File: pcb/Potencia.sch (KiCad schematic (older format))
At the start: 32 parts, among them U3 L298, U4 L298

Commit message: carga de hojas jerarquia
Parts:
- added HS1, HS2: HEATSINK, symbol HEATSINK
- C4, C6, C7, C9: Fabricante (none) -> avx; Provedor (none) -> tme; Ref (none) -> 08055C104K4T2A; Ref_Proveedor (none) -> 08055C104K4T2A
- C5, C8: Provedor (none) -> tme; Ref_Proveedor (none) -> EEVFK1J471M
- D10, D11, D12, D13, D14, D15, D16, D17, D18, D3, D4, D5, D6, D7, D8, D9: Fabricante (none) -> vishay; Provedor (none) -> tme; Ref (none) -> 10MQ100NTRPBF; Ref_Proveedor (none) -> 10MQ100NTRPBF
- R10, R11, R6, R7: Fabricante (none) -> vishay; Potencia (none) -> 0.125W; Provedor (none) -> tme; Ref (none) -> CRCW080510K0FKEA; Ref_Proveedor (none) -> CRCW080510K0FKEA; Tolerancia (none) -> 1%
- R12, R13, R8, R9: Fabricante (none) -> walsin; Potencia (none) -> 1W; Provedor (none) -> tme; Ref (none) -> WW12DR020FTL; Ref_Proveedor (none) -> WW12DR020FTL; Tolerancia (none) -> 1%
- U3, U4: Fabricante (none) -> st; Provedor (none) -> tme; Ref (none) -> L298N; Ref_Proveedor (none) -> L298N
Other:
- moved on the sheet: C4, C5, C6, C7, C8, C9, D10, D11, D12, D13, D14, D15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

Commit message: finalizada realizacion de esquema
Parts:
- added C10, C11, C12, C16, C17, C18, C19, C9: 1,5n, symbol C
- added D15, D16, D17, D18, D3, D4, D5, D6: 1N4148, symbol D
- added R11, R12, R13, R14, R17, R18, R19, R20: 10K, symbol R
- D10: renamed from D6; value D -> 10MQ100
- D11: renamed from D7; value D -> 10MQ100
- D12: renamed from D8; value D -> 10MQ100
- D13: renamed from D9; value D -> 10MQ100
- D14: renamed from D10; value D -> 10MQ100
- D19: renamed from D11; value D -> 10MQ100
- D20: renamed from D12; value D -> 10MQ100
- D21: renamed from D13; value D -> 10MQ100
- D22: renamed from D14; value D -> 10MQ100
- D23: renamed from D15; value D -> 10MQ100
- D24: renamed from D16; value D -> 10MQ100
- D25: renamed from D17; value D -> 10MQ100
- D26: renamed from D18; value D -> 10MQ100
- D7: renamed from D3; value D -> 10MQ100
- D8: renamed from D4; value D -> 10MQ100
- D9: renamed from D5; value D -> 10MQ100
- renumbered C4 to C13, C5 to C14, C6 to C15, C7 to C20, C8 to C21, C9 to C22, R7 to R10, R8 to R15, R9 to R16, R10 to R21, R11 to R22, R12 to R23, R13 to R24, R6 to R9, U3 to U4, U4 to U5
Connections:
- net labels added: Motor1_A_in, Motor1_B_in, Motor2_A_in, Motor2_B_in, Motor3_A_in, Motor3_B_in, Motor4_A_in, Motor4_B_in
- wire segments 90 -> 146
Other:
- moved on the sheet: C13, C14, C15, C20, C21, C22, D10, D11, D12, D13, D14, D19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

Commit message: asociacion de huellas a resistencias y condensadores
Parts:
- C10, C11, C12, C13, C15, C16, C17, C18, C19, C20, C22, C9: footprint (none) -> Capacitors_SMD:C_0805
- C14: Fabricante (none) -> PANASONIC; Ref (none) -> EEVFK1J471M
- R10, R11, R12, R13, R14, R17, R18, R19, R20, R21, R22, R9: footprint (none) -> Resistors_SMD:R_0805
- R15, R16, R23, R24: value R -> 0.02; footprint (none) -> Resistors_SMD:R_1206
- U4, U5: footprint (none) -> MotorDrivers:L298_Multiwatt15V

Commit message: cambiado CI 298N por 298P por altura dentro de posible caja
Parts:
- removed U4, U5: L298, MotorDrivers:L298_Multiwatt15V, symbol L298
- added U4, U5: L298P, MotorDrivers:L298_PowerSO20, symbol L298_SO
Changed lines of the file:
@@
 Comment4 ""
 $EndDescr
-$Comp
-L L298 U4
-U 1 1 5768BA06
-P 2350 3650
-F 0 "U4" H 2900 4400 60  0000 C CNN
-F 1 "L298" H 2900 4550 60  0000 C CNN
-F 2 "MotorDrivers:L298_Multiwatt15V" H 2350 3650 60  0001 C CNN
-F 3 "" H 2350 3650 60  0000 C CNN
-F 4 "st" H 2000 1500 60  0001 C CNN "Fabricante"
-F 5 "L298N" H 2000 1500 60  0001 C CNN "Ref"
-F 6 "~" H 2000 1500 60  0001 C CNN "Potencia"
-F 7 "~" H 2000 1500 60  0001 C CNN "Tolerancia"
-F 8 "tme" H 2000 1500 60  0001 C CNN "Provedor"
-F 9 "L298N" H 2000 1500 60  0001 C CNN "Ref_Proveedor"
-	1    2350 3650
-	1    0    0    -1
-$EndComp
-$Comp
-L L298 U5
-U 1 1 5768BB47
-P 7500 3650
-F 0 "U5" H 8050 4400 60  0000 C CNN
-F 1 "L298" H 8050 4550 60  0000 C CNN
-F 2 "MotorDrivers:L298_Multiwatt15V" H 7500 3650 60  0001 C CNN
-F 3 "" H 7500 3650 60  0000 C CNN
-F 4 "st" H 1800 1500 60  0001 C CNN "Fabricante"
-F 5 "L298N" H 1800 1500 60  0001 C CNN "Ref"
-F 6 "~" H 1800 1500 60  0001 C CNN "Potencia"
-F 7 "~" H 1800 1500 60  0001 C CNN "Tolerancia"
-F 8 "tme" H 1800 1500 60  0001 C CNN "Provedor"
-F 9 "L298N" H 1800 1500 60  0001 C CNN "Ref_Proveedor"
-	1    7500 3650
-	1    0    0    -1
-$EndComp
 Text GLabel 5050 3100 2    60   Input ~ 0
 Motor2-
@@
 	1    0    0    -1
 $EndComp
+$Comp
+L L298_SO U4
+U 1 1 5771BE9E
+P 2350 3650
+F 0 "U4" H 2450 5350 60  0000 C CNN
+F 1 "L298P" H 2900 4500 60  0000 C CNN
+F 2 "MotorDrivers:L298_PowerSO20" H 2350 3650 60  0001 C CNN
+F 3 "" H 2350 3650 60  0000 C CNN
+F 4 "ST" H 2350 3650 60  0001 C CNN "Fabricante"
+F 5 "L298P" H 2350 3650 60  0001 C CNN "Ref"
+F 6 "~" H 2350 3650 60  0001 C CNN "Potencia"
+F 7 "~" H 2350 3650 60  0001 C CNN "Tolerancia"
+F 8 "tme" H 2350 3650 60  0001 C CNN "Provedor"
+F 9 "L298P" H 2350 3650 60  0001 C CNN "Ref_Proveedor"
+	1    2350 3650
+	1    0    0    -1
+$EndComp
+$Comp
+L L298_SO U5
+U 1 1 5771C16D
+P 7500 3650
+F 0 "U5" H 7600 5350 60  0000 C CNN
+F 1 "L298P" H 8050 4500 60  0000 C CNN
+F 2 "MotorDrivers:L298_PowerSO20" H 7500 3650 60  0001 C CNN
+F 3 "" H 7500 3650 60  0000 C CNN
+F 4 "ST" H 7500 3650 60  0001 C CNN "Fabricante"
+F 5 "L298P" H 7500 3650 60  0001 C CNN "Ref"
+F 6 "~" H 7500 3650 60  0001 C CNN "Potencia"
+F 7 "~" H 7500 3650 60  0001 C CNN "Tolerancia"
+F 8 "tme" H 7500 3650 60  0001 C CNN "Provedor"
+F 9 "L298P" H 7500 3650 60  0001 C CNN "Ref_Proveedor"
+	1    7500 3650
+	1    0    0    -1
+$EndComp

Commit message: añadidas asociaciones de condensadores y led
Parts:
- C14: value 470u -> 220u; footprint (none) -> Capacitors_SMD:c_elec_10x10; Ref EEVFK1J471M -> SC1H227M10010VR; Ref_Proveedor EEVFK1J471M -> SC1H227M10010VR
- C21: value 470u -> 220u; footprint (none) -> Capacitors_SMD:c_elec_10x10; Fabricante (none) -> SAMWHA; Ref (none) -> SC1H227M10010VR; Ref_Proveedor EEVFK1J471M -> SC1H227M10010VR
- D10, D11, D12, D13, D14, D19, D20, D21, D22, D23, D24, D25, D26, D7, D8, D9: footprint (none) -> Diodos:DO-214AC
- D15, D16, D17, D18, D3, D4, D5, D6: footprint (none) -> Diodos:SOD-123
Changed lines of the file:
@@
 F 0 "D7" V 3650 2050 50  0000 L CNN
 F 1 "10MQ100" H 3750 1900 50  0000 L CNN
-F 2 "" H 3750 2000 50  0001 C CNN
+F 2 "Diodos:DO-214AC" H 3750 2000 50  0001 C CNN
 F 3 "" H 3750 2000 50  0000 C CNN
 F 4 "vishay" H 3400 1400 60  0001 C CNN "Fabricante"
@@
 F 0 "D9" V 3900 2050 50  0000 L CNN
 F 1 "10MQ100" H 4000 1900 50  0000 L CNN
-F 2 "" H 4000 2000 50  0001 C CNN
+F 2 "Diodos:DO-214AC" H 4000 2000 50  0001 C CNN
 F 3 "" H 4000 2000 50  0000 C CNN
 F 4 "vishay" H 3400 1400 60  0001 C CNN "Fabricante"
@@
 F 0 "D11" V 4150 2050 50  0000 L CNN
 F 1 "10MQ100" H 4250 1900 50  0000 L CNN
-F 2 "" H 4250 2000 50  0001 C CNN
+F 2 "Diodos:DO-214AC" H 4250 2000 50  0001 C CNN
 F 3 "" H 4250 2000 50  0000 C CNN
 F 4 "vishay" H 3400 1400 60  0001 C CNN "Fabricante"
@@
 F 0 "D13" V 4400 2050 50  0000 L CNN
 F 1 "10MQ100" H 4500 1900 50  0000 L CNN
-F 2 "" H 4500 2000 50  0001 C CNN
+F 2 "Diodos:DO-214AC" H 4500 2000 50  0001 C CNN
 F 3 "" H 4500 2000 50  0000 C CNN
 F 4 "vishay" H 3400 1400 60  0001 C CNN "Fabricante"
@@
 F 0 "D8" V 3650 3500 50  0000 L CNN
 F 1 "10MQ100" H 3750 3350 50  0000 L CNN
-F 2 "" H 3750 3450 50  0001 C CNN
+F 2 "Diodos:DO-214AC" H 3750 3450 50  0001 C CNN
 F 3 "" H 3750 3450 50  0000 C CNN
 F 4 "vishay" H 3400 1400 60  0001 C CNN "Fabricante"
@@
 F 0 "D10" V 3900 3500 50  0000 L CNN
 F 1 "10MQ100" H 4000 3350 50  0000 L CNN
-F 2 "" H 4000 3450 50  0001 C CNN
+F 2 "Diodos:DO-214AC" H 4000 3450 50  0001 C CNN
 F 3 "" H 4000 3450 50  0000 C CNN
 F 4 "vishay" H 3400 1400 60  0001 C CNN "Fabricante"
@@
 F 0 "D12" V 4150 3500 50  0000 L CNN
 F 1 "10MQ100" H 4250 3350 50  0000 L CNN
-F 2 "" H 4250 3450 50  0001 C CNN
+F 2 "Diodos:DO-214AC" H 4250 3450 50  0001 C CNN
 F 3 "" H 4250 3450 50  0000 C CNN
 F 4 "vishay" H 3400 1400 60  0001 C CNN "Fabricante"
@@
 F 0 "D14" V 4400 3500 50  0000 L CNN
 F 1 "10MQ100" H 4500 3350 50  0000 L CNN
-F 2 "" H 4500 3450 50  0001 C CNN
+F 2 "Diodos:DO-214AC" H 4500 3450 50  0001 C CNN
 F 3 "" H 4500 3450 50  0000 C CNN
 F 4 "vishay" H 3400 1400 60  0001 C CNN "Fabricante"
@@
 P 3000 1400
 F 0 "C14" H 3118 1446 50  0000 L CNN
-F 1 "470u" H 3118 1355 50  0000 L CNN
-F 2 "" H 3038 1250 50  0001 C CNN
+F 1 "220u" H 3118 1355 50  0000 L CNN
+F 2 "Capacitors_SMD:c_elec_10x10" H 3038 1250 50  0001 C CNN
 F 3 "" H 3000 1400 50  0000 C CNN
 F 4 "PANASONIC" H 3000 1400 60  0001 C CNN "Fabricante"
-F 5 "EEVFK1J471M" H 3000 1400 60  0001 C CNN "Ref"
+F 5 "SC1H227M10010VR" H 3000 1400 60  0001 C CNN "Ref"
 F 6 "~" H 3000 1400 60  0001 C CNN "Potencia"
 F 7 "~" H 3000 1400 60  0001 C CNN "Tolerancia"
 F 8 "tme" H 3000 1400 60  0001 C CNN "Provedor"
-F 9 "EEVFK1J471M" H 3000 1400 60  0001 C CNN "Ref_Proveedor"
+F 9 "SC1H227M10010VR" H 3000 1400 60  0001 C CNN "Ref_Proveedor"
 	1    3000 1400
 	1    0    0    -1
@@
 F 0 "D19" V 8850 2050 50  0000 L CNN
 F 1 "10MQ100" H 8950 1900 50  0000 L CNN
-F 2 "" H 8950 2000 50  0001 C CNN
+F 2 "Diodos:DO-214AC" H 8950 2000 50  0001 C CNN
 F 3 "" H 8950 2000 50  0000 C CNN
 F 4 "vishay" H 3200 1350 60  0001 C CNN "Fabricante"
@@
 F 0 "D21" V 9100 2050 50  0000 L CNN
 F 1 "10MQ100" H 9200 1900 50  0000 L CNN
-F 2 "" H 9200 2000 50  0001 C CNN
+F 2 "Diodos:DO-214AC" H 9200 2000 50  0001 C CNN
 F 3 "" H 9200 2000 50  0000 C CNN
 F 4 "vishay" H 3200 1350 60  0001 C CNN "Fabricante"
@@
 F 0 "D23" V 9350 2050 50  0000 L CNN
 F 1 "10MQ100" H 9450 1900 50  0000 L CNN
-F 2 "" H 9450 2000 50  0001 C CNN
+F 2 "Diodos:DO-214AC" H 9450 2000 50  0001 C CNN
 F 3 "" H 9450 2000 50  0000 C CNN
 F 4 "vishay" H 3200 1350 60  0001 C CNN "Fabricante"
@@
 F 0 "D25" V 9600 2050 50  0000 L CNN
 F 1 "10MQ100" H 9700 1900 50  0000 L CNN
-F 2 "" H 9700 2000 50  0001 C CNN
+F 2 "Diodos:DO-214AC" H 9700 2000 50  0001 C CNN
 F 3 "" H 9700 2000 50  0000 C CNN
 F 4 "vishay" H 3200 1350 60  0001 C CNN "Fabricante"
@@
 F 0 "D20" V 8850 3500 50  0000 L CNN
 F 1 "10MQ100" H 8950 3350 50  0000 L CNN
-F 2 "" H 8950 3450 50  0001 C CNN
+F 2 "Diodos:DO-214AC" H 8950 3450 50  0001 C CNN
 F 3 "" H 8950 3450 50  0000 C CNN
 F 4 "vishay" H 3200 1350 60  0001 C CNN "Fabricante"
@@
 F 0 "D22" V 9100 3500 50  0000 L CNN
 F 1 "10MQ100" H 9200 3350 50  0000 L CNN
-F 2 "" H 9200 3450 50  0001 C CNN
+F 2 "Diodos:DO-214AC" H 9200 3450 50  0001 C CNN
 F 3 "" H 9200 3450 50  0000 C CNN
 F 4 "vishay" H 3200 1350 60  0001 C CNN "Fabricante"
@@
 F 0 "D24" V 9350 3500 50  0000 L CNN
 F 1 "10MQ100" H 9450 3350 50  0000 L CNN
-F 2 "" H 9450 3450 50  0001 C CNN
+F 2 "Diodos:DO-214AC" H 9450 3450 50  0001 C CNN
 F 3 "" H 9450 3450 50  0000 C CNN
 F 4 "vishay" H 3200 1350 60  0001 C CNN "Fabricante"
@@
 F 0 "D26" V 9600 3500 50  0000 L CNN
 F 1 "10MQ100" H 9700 3350 50  0000 L CNN
-F 2 "" H 9700 3450 50  0001 C CNN
+F 2 "Diodos:DO-214AC" H 9700 3450 50  0001 C CNN
 F 3 "" H 9700 3450 50  0000 C CNN
 F 4 "vishay" H 3200 1350 60  0001 C CNN "Fabricante"
@@
 P 8150 1450
 F 0 "C21" H 8268 1496 50  0000 L CNN
-F 1 "470u" H 8268 1405 50  0000 L CNN
-F 2 "" H 8188 1300 50  0001 C CNN
+F 1 "220u" H 8268 1405 50  0000 L CNN
+F 2 "Capacitors_SMD:c_elec_10x10" H 8188 1300 50  0001 C CNN
 F 3 "" H 8150 1450 50  0000 C CNN
-F 4 "~" H 8150 1450 60  0001 C CNN "Fabricante"
-F 5 "~" H 8150 1450 60  0001 C CNN "Ref"
+F 4 "SAMWHA" H 8150 1450 60  0001 C CNN "Fabricante"
+F 5 "SC1H227M10010VR" H 8150 1450 60  0001 C CNN "Ref"
 F 6 "~" H 8150 1450 60  0001 C CNN "Potencia"
 F 7 "~" H 8150 1450 60  0001 C CNN "Tolerancia"
 F 8 "tme" H 8150 1450 60  0001 C CNN "Provedor"
-F 9 "EEVFK1J471M" H 8150 1450 60  0001 C CNN "Ref_Proveedor"
+F 9 "SC1H227M10010VR" H 8150 1450 60  0001 C CNN "Ref_Proveedor"
 	1    8150 1450
 	1    0    0    -1
@@
 F 0 "D3" H 1650 5700 50  0000 C CNN
 F 1 "1N4148" H 1800 5850 50  0000 C CNN
-F 2 "" H 1800 5750 50  0001 C CNN
+F 2 "Diodos:SOD-123" H 1800 5750 50  0001 C CNN
 F 3 "" H 1800 5750 50  0000 C CNN
 F 4 "DIOTEC SEMICONDUCTOR" H 1800 5750 60  0001 C CNN "Fabricante"
@@
 F 0 "D4" H 1650 6200 50  0000 C CNN
 F 1 "1N4148" H 1800 6350 50  0000 C CNN
-F 2 "" H 1800 6250 50  0001 C CNN
+F 2 "Diodos:SOD-123" H 1800 6250 50  0001 C CNN
 F 3 "" H 1800 6250 50  0000 C CNN
 F 4 "DIOTEC SEMICONDUCTOR" H 1800 5750 60  0001 C CNN "Fabricante"
@@
 F 0 "D5" H 1650 6750 50  0000 C CNN
 F 1 "1N4148" H 1800 6900 50  0000 C CNN
-F 2 "" H 1800 6800 50  0001 C CNN
+F 2 "Diodos:SOD-123" H 1800 6800 50  0001 C CNN
 F 3 "" H 1800 6800 50  0000 C CNN
 F 4 "DIOTEC SEMICONDUCTOR" H 1800 5750 60  0001 C CNN "Fabricante"
@@
 F 0 "D6" H 1650 7250 50  0000 C CNN
 F 1 "1N4148" H 1800 7400 50  0000 C CNN
-F 2 "" H 1800 7300 50  0001 C CNN
+F 2 "Diodos:SOD-123" H 1800 7300 50  0001 C CNN
 F 3 "" H 1800 7300 50  0000 C CNN
 F 4 "DIOTEC SEMICONDUCTOR" H 1800 5750 60  0001 C CNN "Fabricante"
@@
 F 0 "D15" H 4700 5700 50  0000 C CNN
 F 1 "1N4148" H 4850 5850 50  0000 C CNN
-F 2 "" H 4850 5750 50  0001 C CNN
+F 2 "Diodos:SOD-123" H 4850 5750 50  0001 C CNN
 F 3 "" H 4850 5750 50  0000 C CNN
 F 4 "DIOTEC SEMICONDUCTOR" H 1800 5750 60  0001 C CNN "Fabricante"
@@
 F 0 "D16" H 4700 6200 50  0000 C CNN
 F 1 "1N4148" H 4850 6350 50  0000 C CNN
-F 2 "" H 4850 6250 50  0001 C CNN
+F 2 "Diodos:SOD-123" H 4850 6250 50  0001 C CNN
 F 3 "" H 4850 6250 50  0000 C CNN
 F 4 "DIOTEC SEMICONDUCTOR" H 1800 5750 60  0001 C CNN "Fabricante"
@@
 F 0 "D17" H 4700 6750 50  0000 C CNN
 F 1 "1N4148" H 4850 6900 50  0000 C CNN
-F 2 "" H 4850 6800 50  0001 C CNN
+F 2 "Diodos:SOD-123" H 4850 6800 50  0001 C CNN
 F 3 "" H 4850 6800 50  0000 C CNN
 F 4 "DIOTEC SEMICONDUCTOR" H 1800 5750 60  0001 C CNN "Fabricante"
@@
 F 0 "D18" H 4700 7250 50  0000 C CNN
 F 1 "1N4148" H 4850 7400 50  0000 C CNN
-F 2 "" H 4850 7300 50  0001 C CNN
+F 2 "Diodos:SOD-123" H 4850 7300 50  0001 C CNN
 F 3 "" H 4850 7300 50  0000 C CNN
 F 4 "DIOTEC SEMICONDUCTOR" H 1800 5750 60  0001 C CNN "Fabricante"

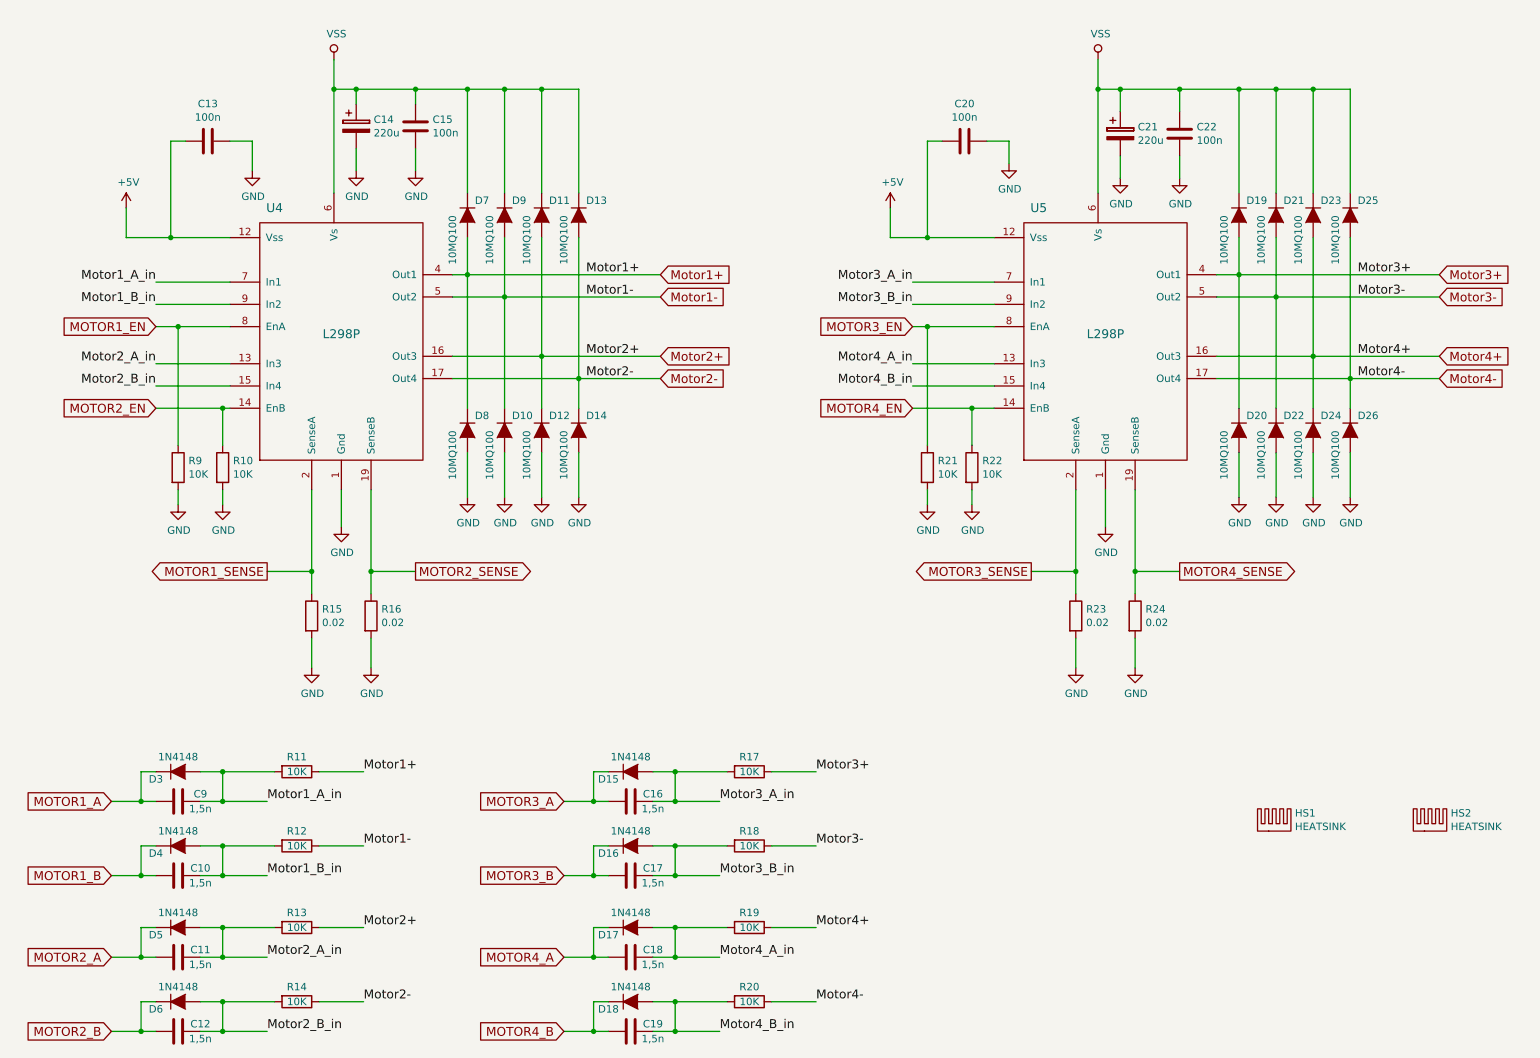
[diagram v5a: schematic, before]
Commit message: se añaden optos para E/S y cristal
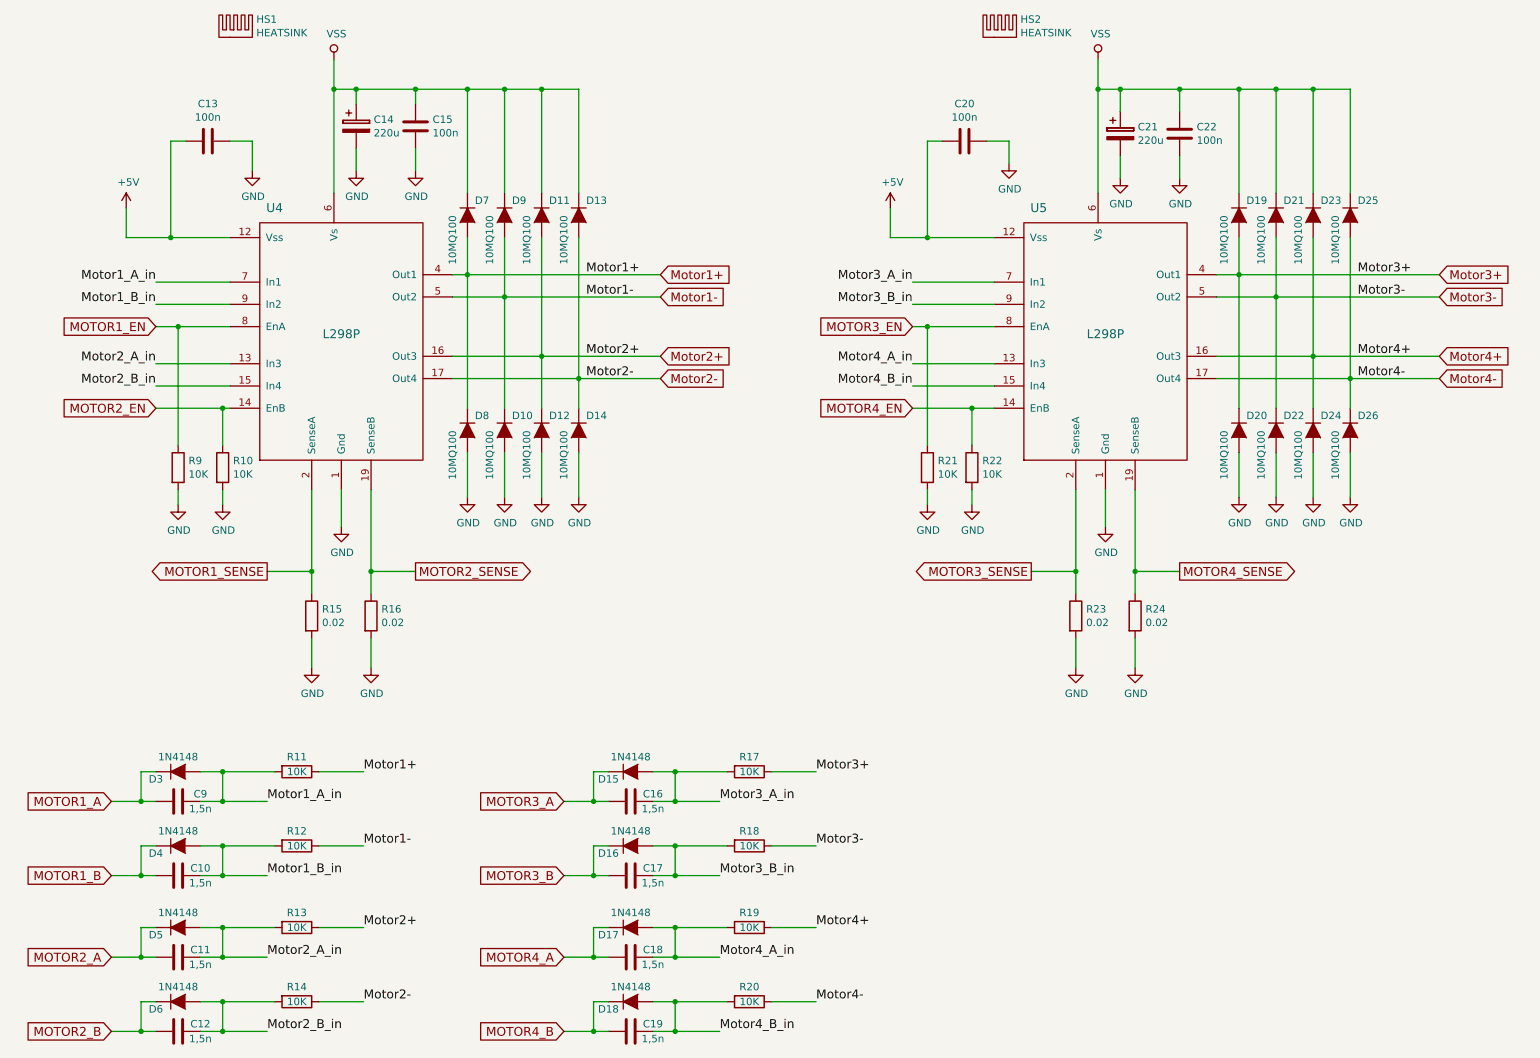
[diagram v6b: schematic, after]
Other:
- moved on the sheet: HS1, HS2
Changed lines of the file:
@@
 LIBS:Opamp
 LIBS:Traco
+LIBS:Optoacoplados
 LIBS:ATMEGA328_Motor_Board-cache
 EELAYER 25 0
@@
 $Descr A4 11693 8268
 encoding utf-8
-Sheet 3 6
+Sheet 3 7
 Title ""
 Date ""
@@
 L HEATSINK HS1
 U 1 1 576B1B70
-P 9200 6150
-F 0 "HS1" H 9327 6271 50  0000 L CNN
-F 1 "HEATSINK" H 9327 6180 50  0000 L CNN
-F 2 "" H 9200 6150 50  0001 C CNN
-F 3 "" H 9200 6150 50  0000 C CNN
-F 4 "AAVID THERMALLOY" H 9200 6150 60  0001 C CNN "Fabricante"
-F 5 "ML33" H 9200 6150 60  0001 C CNN "Ref"
-F 6 "~" H 9200 6150 60  0001 C CNN "Potencia"
-F 7 "~" H 9200 6150 60  0001 C CNN "Tolerancia"
-F 8 "rs" H 9200 6150 60  0001 C CNN "Provedor"
-F 9 "712-4263" H 9200 6150 60  0001 C CNN "Ref_Proveedor"
-	1    9200 6150
+P 2200 800
+F 0 "HS1" H 2327 921 50  0000 L CNN
+F 1 "HEATSINK" H 2327 830 50  0000 L CNN
+F 2 "" H 2200 800 50  0001 C CNN
+F 3 "" H 2200 800 50  0000 C CNN
+F 4 "AAVID THERMALLOY" H 2200 800 60  0001 C CNN "Fabricante"
+F 5 "ML33" H 2200 800 60  0001 C CNN "Ref"
+F 6 "~" H 2200 800 60  0001 C CNN "Potencia"
+F 7 "~" H 2200 800 60  0001 C CNN "Tolerancia"
+F 8 "rs" H 2200 800 60  0001 C CNN "Provedor"
+F 9 "712-4263" H 2200 800 60  0001 C CNN "Ref_Proveedor"
+	1    2200 800
 	1    0    0    -1
 $EndComp
@@
 L HEATSINK HS2
 U 1 1 576B202D
-P 10250 6150
-F 0 "HS2" H 10377 6271 50  0000 L CNN
-F 1 "HEATSINK" H 10377 6180 50  0000 L CNN
-F 2 "" H 10250 6150 50  0001 C CNN
-F 3 "" H 10250 6150 50  0000 C CNN
-F 4 "AAVID THERMALLOY" H 10250 6150 60  0001 C CNN "Fabricante"
-F 5 "ML33" H 10250 6150 60  0001 C CNN "Ref"
-F 6 "~" H 10250 6150 60  0001 C CNN "Potencia"
-F 7 "~" H 10250 6150 60  0001 C CNN "Tolerancia"
-F 8 "rs" H 10250 6150 60  0001 C CNN "Provedor"
-F 9 "712-4263" H 10250 6150 60  0001 C CNN "Ref_Proveedor"
-	1    10250 6150
-	1    0    0    -1
-$EndComp
+P 7350 800
+F 0 "HS2" H 7477 921 50  0000 L CNN
+F 1 "HEATSINK" H 7477 830 50  0000 L CNN
+F 2 "" H 7350 800 50  0001 C CNN
+F 3 "" H 7350 800 50  0000 C CNN
+F 4 "AAVID THERMALLOY" H 7350 800 60  0001 C CNN "Fabricante"
+F 5 "ML33" H 7350 800 60  0001 C CNN "Ref"
+F 6 "~" H 7350 800 60  0001 C CNN "Potencia"
+F 7 "~" H 7350 800 60  0001 C CNN "Tolerancia"
+F 8 "rs" H 7350 800 60  0001 C CNN "Provedor"
+F 9 "712-4263" H 7350 800 60  0001 C CNN "Ref_Proveedor"
+	1    7350 800
+	1    0    0    -1
+$EndComp
